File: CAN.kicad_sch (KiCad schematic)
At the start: 7 parts, among them U1 TCAN1462VDRQ1, U2 ESDCAN24-2BLY

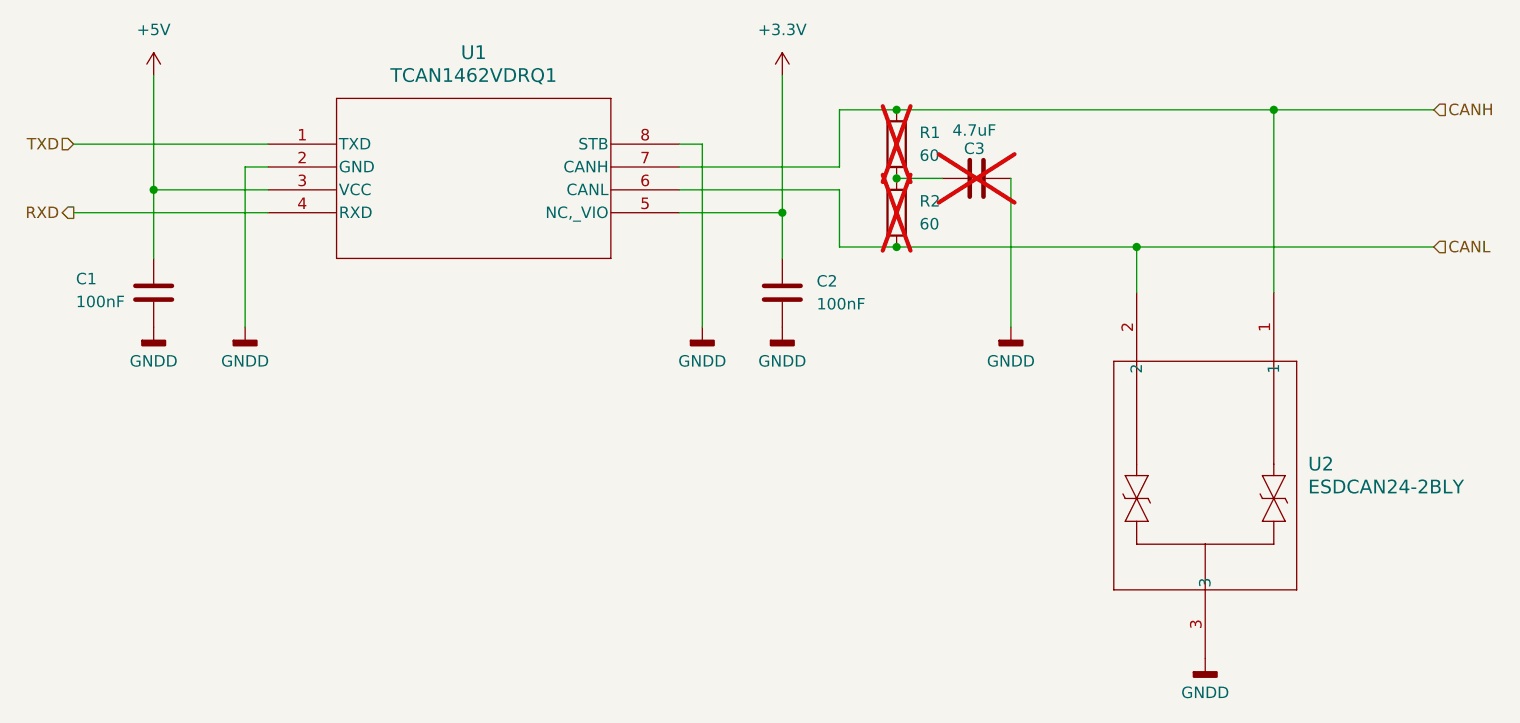
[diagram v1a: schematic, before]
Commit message: assigned footprints, some minor schematic stuff, started layout
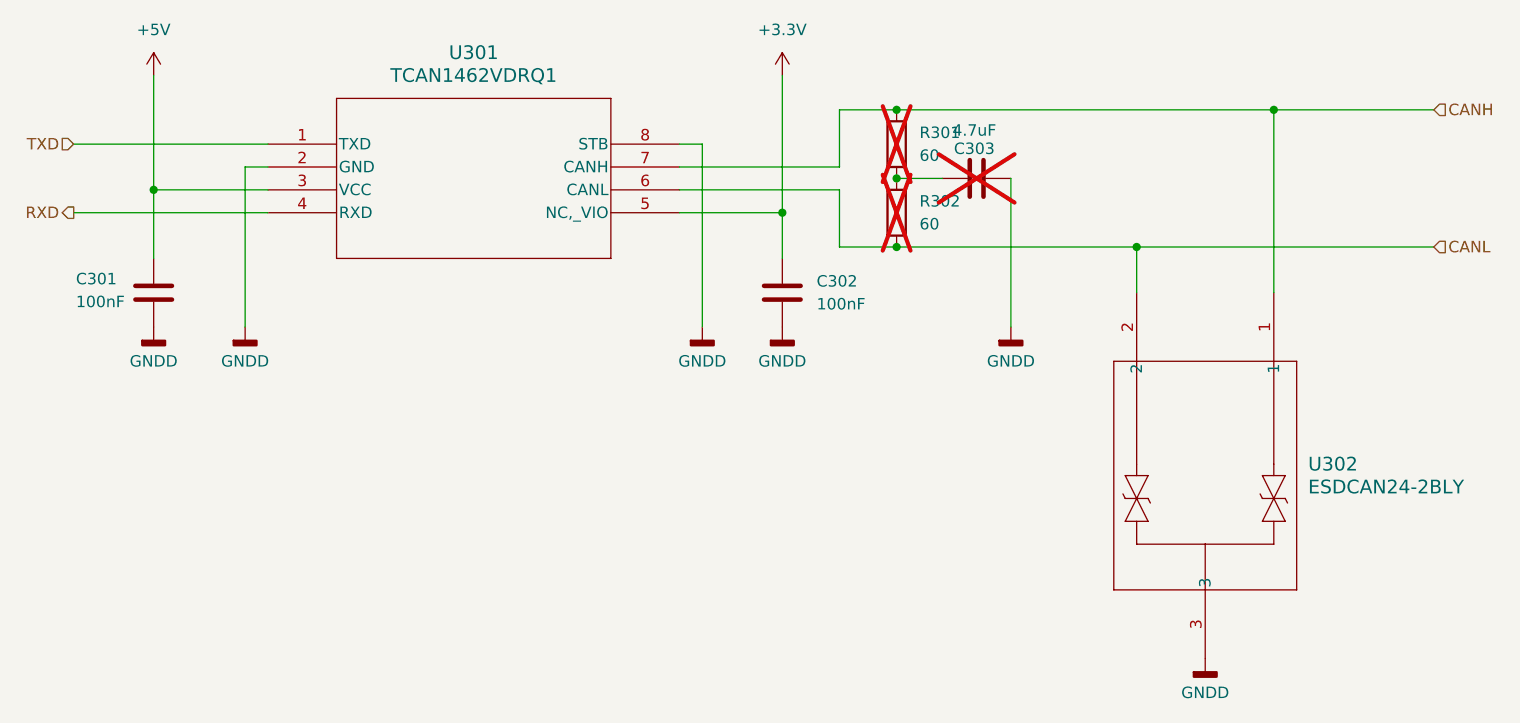
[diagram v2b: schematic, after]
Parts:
- C301: renamed from C1; footprint (none) -> Capacitor_SMD:C_0603_1608Metric
- C302: renamed from C2; footprint (none) -> Capacitor_SMD:C_0603_1608Metric
- C303: renamed from C3; footprint (none) -> Capacitor_SMD:C_0603_1608Metric
- R301: renamed from R1; footprint (none) -> Resistor_SMD:R_0603_1608Metric
- R302: renamed from R2; footprint (none) -> Resistor_SMD:R_0603_1608Metric
- U301: renamed from U1; footprint SOIC8_D_TEX -> footprints:SOIC8_D_TEX
- U302: renamed from U2; footprint SOT_24-2BLY_STM -> footprints:SOT_24-2BLY_STM
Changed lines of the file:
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@@
 		(dnp no)
 		(fields_autoplaced yes)
-		(property "Reference" "#PWR024"
+		(property "Reference" "#PWR0304"
 			(at 143.51 114.3 0)
 			(hide yes)
@@
 			(project "LV_DCDC"
 				(path "/ccad4640-78c7-423b-83df-3ec0b90aa2b3/f9342e9a-2c81-4a9f-bedf-76ac3e437a63/a5b38994-2bc4-4831-8336-eb0df1055128"
-					(reference "#PWR024")
+					(reference "#PWR0304")
 					(unit 1)
 				)
@@
 		(in_pos_files yes)
 		(dnp yes)
-		(property "Reference" "C3"
+		(property "Reference" "C303"
 			(at 173.736 88.138 90)
 			(show_name no)
@@
 			)
 		)
-		(property "Footprint" ""
+		(property "Footprint" "Capacitor_SMD:C_0603_1608Metric"
 			(at 170.18 92.4052 0)
 			(hide yes)
@@
 			(project "LV_DCDC"
 				(path "/ccad4640-78c7-423b-83df-3ec0b90aa2b3/f9342e9a-2c81-4a9f-bedf-76ac3e437a63/a5b38994-2bc4-4831-8336-eb0df1055128"
-					(reference "C3")
+					(reference "C303")
 					(unit 1)
 				)
@@
 		(dnp no)
 		(fields_autoplaced yes)
-		(property "Reference" "#PWR06"
+		(property "Reference" "#PWR0305"
 			(at 152.4 83.82 0)
 			(hide yes)
@@
 			(project "LV_DCDC"
 				(path "/ccad4640-78c7-423b-83df-3ec0b90aa2b3/f9342e9a-2c81-4a9f-bedf-76ac3e437a63/a5b38994-2bc4-4831-8336-eb0df1055128"
-					(reference "#PWR06")
+					(reference "#PWR0305")
 					(unit 1)
 				)
@@
 		(dnp yes)
 		(fields_autoplaced yes)
-		(property "Reference" "R2"
+		(property "Reference" "R302"
 			(at 167.64 93.9799 0)
 			(show_name no)
@@
 			)
 		)
-		(property "Footprint" ""
+		(property "Footprint" "Resistor_SMD:R_0603_1608Metric"
 			(at 163.322 95.25 90)
 			(hide yes)
@@
 			(project "LV_DCDC"
 				(path "/ccad4640-78c7-423b-83df-3ec0b90aa2b3/f9342e9a-2c81-4a9f-bedf-76ac3e437a63/a5b38994-2bc4-4831-8336-eb0df1055128"
-					(reference "R2")
+					(reference "R302")
 					(unit 1)
 				)
@@
 		(dnp yes)
 		(fields_autoplaced yes)
-		(property "Reference" "R1"
+		(property "Reference" "R301"
 			(at 167.64 86.3599 0)
 			(show_name no)
@@
 			)
 		)
-		(property "Footprint" ""
+		(property "Footprint" "Resistor_SMD:R_0603_1608Metric"
 			(at 163.322 87.63 90)
 			(hide yes)
@@
 			(project "LV_DCDC"
 				(path "/ccad4640-78c7-423b-83df-3ec0b90aa2b3/f9342e9a-2c81-4a9f-bedf-76ac3e437a63/a5b38994-2bc4-4831-8336-eb0df1055128"
-					(reference "R1")
+					(reference "R301")
 					(unit 1)
 				)
@@
 		(dnp no)
 		(fields_autoplaced yes)
-		(property "Reference" "#PWR05"
+		(property "Reference" "#PWR0301"
 			(at 82.55 83.82 0)
 			(hide yes)
@@
 			(project "LV_DCDC"
 				(path "/ccad4640-78c7-423b-83df-3ec0b90aa2b3/f9342e9a-2c81-4a9f-bedf-76ac3e437a63/a5b38994-2bc4-4831-8336-eb0df1055128"
-					(reference "#PWR05")
+					(reference "#PWR0301")
 					(unit 1)
 				)
@@
 		(in_pos_files yes)
 		(dnp no)
-		(property "Reference" "C1"
+		(property "Reference" "C301"
 			(at 73.914 102.616 0)
 			(show_name no)
@@
 			)
 		)
-		(property "Footprint" ""
+		(property "Footprint" "Capacitor_SMD:C_0603_1608Metric"
 			(at 83.5152 107.95 0)
 			(hide yes)
@@
 			(project "LV_DCDC"
 				(path "/ccad4640-78c7-423b-83df-3ec0b90aa2b3/f9342e9a-2c81-4a9f-bedf-76ac3e437a63/a5b38994-2bc4-4831-8336-eb0df1055128"
-					(reference "C1")
+					(reference "C301")
 					(unit 1)
 				)
@@
 		(dnp no)
 		(fields_autoplaced yes)
-		(property "Reference" "#PWR023"
+		(property "Reference" "#PWR0303"
 			(at 92.71 114.3 0)
 			(hide yes)
@@
 			(project "LV_DCDC"
 				(path "/ccad4640-78c7-423b-83df-3ec0b90aa2b3/f9342e9a-2c81-4a9f-bedf-76ac3e437a63/a5b38994-2bc4-4831-8336-eb0df1055128"
-					(reference "#PWR023")
+					(reference "#PWR0303")
 					(unit 1)
 				)
@@
 		(dnp no)
 		(fields_autoplaced yes)
-		(property "Reference" "#PWR015"
+		(property "Reference" "#PWR0308"
 			(at 199.39 151.13 0)
 			(hide yes)
@@
 			(project "LV_DCDC"
 				(path "/ccad4640-78c7-423b-83df-3ec0b90aa2b3/f9342e9a-2c81-4a9f-bedf-76ac3e437a63/a5b38994-2bc4-4831-8336-eb0df1055128"
-					(reference "#PWR015")
+					(reference "#PWR0308")
 					(unit 1)
 				)
@@
 		(dnp no)
 		(fields_autoplaced yes)
-		(property "Reference" "C2"
+		(property "Reference" "C302"
 			(at 156.21 102.8699 0)
 			(show_name no)
@@
 			)
 		)
-		(property "Footprint" ""
+		(property "Footprint" "Capacitor_SMD:C_0603_1608Metric"
 			(at 153.3652 107.95 0)
 			(hide yes)
@@
 			(project "LV_DCDC"
 				(path "/ccad4640-78c7-423b-83df-3ec0b90aa2b3/f9342e9a-2c81-4a9f-bedf-76ac3e437a63/a5b38994-2bc4-4831-8336-eb0df1055128"
-					(reference "C2")
+					(reference "C302")
 					(unit 1)
 				)
@@
 		(dnp no)
 		(fields_autoplaced yes)
-		(property "Reference" "U2"
+		(property "Reference" "U302"
 			(at 210.82 123.1899 90)
 			(show_name no)
@@
 			)
 		)
-		(property "Footprint" "SOT_24-2BLY_STM"
+		(property "Footprint" "footprints:SOT_24-2BLY_STM"
 			(at 207.01 104.14 0)
 			(hide yes)
@@
 			(project "LV_DCDC"
 				(path "/ccad4640-78c7-423b-83df-3ec0b90aa2b3/f9342e9a-2c81-4a9f-bedf-76ac3e437a63/a5b38994-2bc4-4831-8336-eb0df1055128"
-					(reference "U2")
+					(reference "U302")
 					(unit 1)
 				)
@@
 		(dnp no)
 		(fields_autoplaced yes)
-		(property "Reference" "#PWR017"
+		(property "Reference" "#PWR0302"
 			(at 82.55 114.3 0)
 			(hide yes)
@@
 			(project "LV_DCDC"
 				(path "/ccad4640-78c7-423b-83df-3ec0b90aa2b3/f9342e9a-2c81-4a9f-bedf-76ac3e437a63/a5b38994-2bc4-4831-8336-eb0df1055128"
-					(reference "#PWR017")
+					(reference "#PWR0302")
 					(unit 1)
 				)
@@
 		(dnp no)
 		(fields_autoplaced yes)
-		(property "Reference" "#PWR016"
+		(property "Reference" "#PWR0306"
 			(at 152.4 114.3 0)
 			(hide yes)
@@
 			(project "LV_DCDC"
 				(path "/ccad4640-78c7-423b-83df-3ec0b90aa2b3/f9342e9a-2c81-4a9f-bedf-76ac3e437a63/a5b38994-2bc4-4831-8336-eb0df1055128"
-					(reference "#PWR016")
+					(reference "#PWR0306")
 					(unit 1)
 				)
@@
 		(dnp no)
 		(fields_autoplaced yes)
-		(property "Reference" "U1"
+		(property "Reference" "U301"
 			(at 118.11 77.47 0)
 			(show_name no)
@@
 			)
 		)
-		(property "Footprint" "SOIC8_D_TEX"
+		(property "Footprint" "footprints:SOIC8_D_TEX"
 			(at 95.25 87.63 0)
 			(hide yes)
@@
 			(project "LV_DCDC"
 				(path "/ccad4640-78c7-423b-83df-3ec0b90aa2b3/f9342e9a-2c81-4a9f-bedf-76ac3e437a63/a5b38994-2bc4-4831-8336-eb0df1055128"
-					(reference "U1")
+					(reference "U301")
 					(unit 1)
 				)
@@
 		(dnp no)
 		(fields_autoplaced yes)
-		(property "Reference" "#PWR018"
+		(property "Reference" "#PWR0307"
 			(at 177.8 114.3 0)
 			(hide yes)
@@
 			(project "LV_DCDC"
 				(path "/ccad4640-78c7-423b-83df-3ec0b90aa2b3/f9342e9a-2c81-4a9f-bedf-76ac3e437a63/a5b38994-2bc4-4831-8336-eb0df1055128"
-					(reference "#PWR018")
-					(unit 1)
-				)
+					(reference "#PWR0307")
+					(unit 1)
+				)

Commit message: progress on layout in general, minor tweaks to schemas
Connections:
- net CANH: now also U302.2; no longer U302.1
- net CANL: now also U302.1; no longer U302.2
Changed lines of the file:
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@@
+	)
+	(junction
+		(at 207.01 99.06)
+		(diameter 0)
+		(color 0 0 0 0)
 	)
 	(junction
@@
 	)
 	(junction
-		(at 191.77 99.06)
+		(at 191.77 83.82)
 		(diameter 0)
 		(color 0 0 0 0)
@@
 		(color 0 0 0 0)
 	)
-	(junction
-		(at 207.01 83.82)
-		(diameter 0)
-		(color 0 0 0 0)
-	)
 	(wire
 		(pts
@@
 	(wire
 		(pts
-			(xy 191.77 99.06) (xy 191.77 104.14)
-		)
-		(stroke
-			(width 0)
-			(type default)
-		)
-	)
-	(wire
-		(pts
 			(xy 158.75 83.82) (xy 165.1 83.82)
 		)
@@
 	(wire
 		(pts
-			(xy 207.01 83.82) (xy 224.79 83.82)
+			(xy 165.1 83.82) (xy 191.77 83.82)
 		)
 		(stroke
@@
 	(wire
 		(pts
+			(xy 207.01 99.06) (xy 207.01 104.14)
+		)
+		(stroke
+			(width 0)
+			(type default)
+		)
+	)
+	(wire
+		(pts
 			(xy 92.71 107.95) (xy 92.71 90.17)
 		)
@@
 	(wire
 		(pts
-			(xy 165.1 83.82) (xy 207.01 83.82)
-		)
-		(stroke
-			(width 0)
-			(type default)
-		)
-	)
-	(wire
-		(pts
 			(xy 140.97 95.25) (xy 152.4 95.25)
 		)
@@
 	(wire
 		(pts
-			(xy 165.1 99.06) (xy 191.77 99.06)
-		)
-		(stroke
-			(width 0)
-			(type default)
-		)
-	)
-	(wire
-		(pts
-			(xy 207.01 83.82) (xy 207.01 104.14)
+			(xy 191.77 83.82) (xy 224.79 83.82)
+		)
+		(stroke
+			(width 0)
+			(type default)
+		)
+	)
+	(wire
+		(pts
+			(xy 191.77 83.82) (xy 191.77 104.14)
 		)
 		(stroke
@@
 	(wire
 		(pts
-			(xy 191.77 99.06) (xy 224.79 99.06)
-		)
-		(stroke
+			(xy 165.1 99.06) (xy 207.01 99.06)
+		)
+		(stroke
+			(width 0)
+			(type default)
+		)
+	)
+	(wire
+		(pts
+			(xy 207.01 99.06) (xy 224.79 99.06)
+		)
+		(stroke
